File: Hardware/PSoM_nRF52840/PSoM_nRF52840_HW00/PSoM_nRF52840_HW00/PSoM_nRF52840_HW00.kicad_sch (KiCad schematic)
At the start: 0 parts

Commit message: started nrf52 schematic
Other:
- sheet 400_ESP32 renamed 400_nRF52840
- title: PSoM - ESP S3 -> PSoM - nRF52840

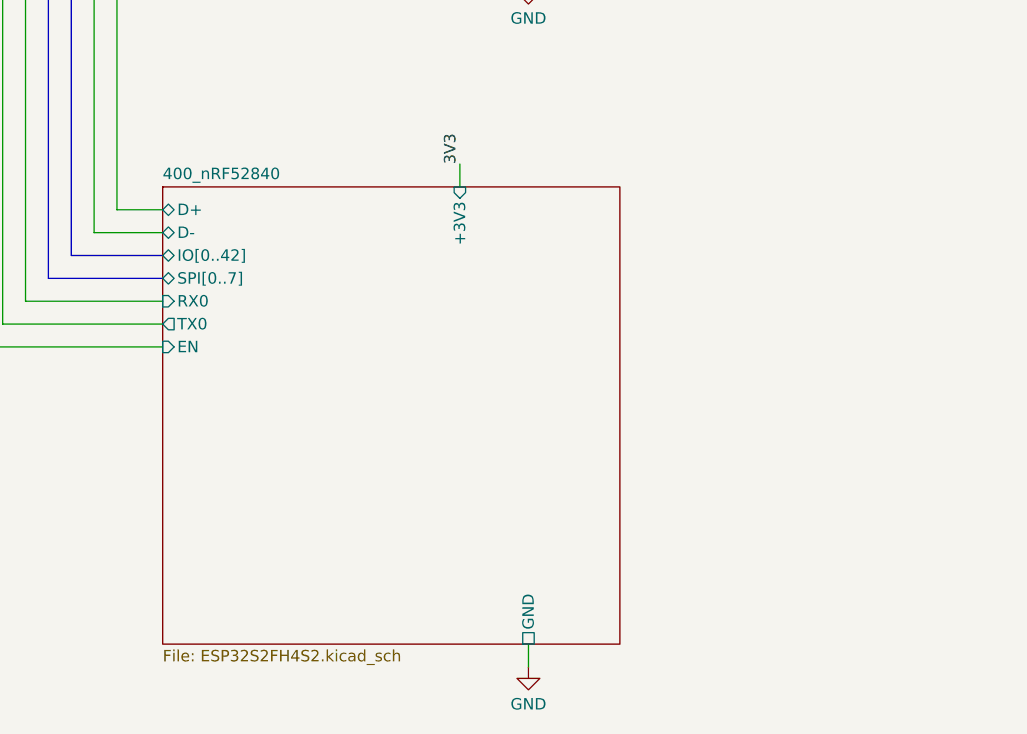
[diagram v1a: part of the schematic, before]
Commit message: nrf schematic ongoing
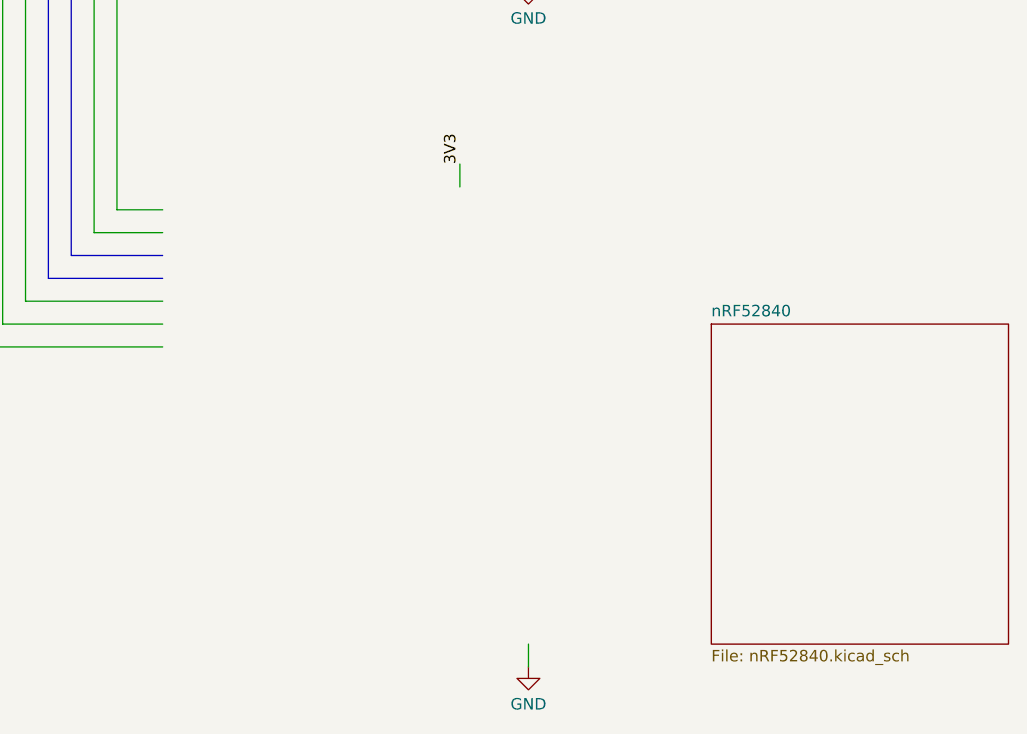
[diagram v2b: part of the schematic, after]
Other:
- removed sheet 400_nRF52840
- added sheet nRF52840 (nRF52840.kicad_sch)
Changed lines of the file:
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@@
 	)
 	(sheet
-		(at 127 101.6)
-		(size 50.8 50.8)
+		(at 187.96 116.84)
+		(size 33.02 35.56)
 		(fields_autoplaced yes)
 		(stroke
@@
 			(color 0 0 0 0.0000)
 		)
-		(property "Sheetname" "400_nRF52840"
-			(at 127 100.8884 0)
+		(property "Sheetname" "nRF52840"
+			(at 187.96 116.1284 0)
 			(effects
 				(font
@@
 			)
 		)
-		(property "Sheetfile" "ESP32S2FH4S2.kicad_sch"
-			(at 127 152.9846 0)
+		(property "Sheetfile" "nRF52840.kicad_sch"
+			(at 187.96 152.9846 0)
 			(effects
 				(font
@@
 			)
 		)
-		(pin "D-" bidirectional
-			(at 127 106.68 180)
-			(effects
-				(font
-					(size 1.27 1.27)
-				)
-				(justify left)
-			)
-		)
-		(pin "+3V3" input
-			(at 160.02 101.6 90)
-			(effects
-				(font
-					(size 1.27 1.27)
-				)
-				(justify right)
-			)
-		)
-		(pin "D+" bidirectional
-			(at 127 104.14 180)
-			(effects
-				(font
-					(size 1.27 1.27)
-				)
-				(justify left)
-			)
-		)
-		(pin "GND" passive
-			(at 167.64 152.4 270)
-			(effects
-				(font
-					(size 1.27 1.27)
-				)
-				(justify left)
-			)
-		)
-		(pin "IO[0..42]" bidirectional
-			(at 127 109.22 180)
-			(effects
-				(font
-					(size 1.27 1.27)
-				)
-				(justify left)
-			)
-		)
-		(pin "RX0" input
-			(at 127 114.3 180)
-			(effects
-				(font
-					(size 1.27 1.27)
-				)
-				(justify left)
-			)
-		)
-		(pin "TX0" output
-			(at 127 116.84 180)
-			(effects
-				(font
-					(size 1.27 1.27)
-				)
-				(justify left)
-			)
-		)
-		(pin "SPI[0..7]" bidirectional
-			(at 127 111.76 180)
-			(effects
-				(font
-					(size 1.27 1.27)
-				)
-				(justify left)
-			)
-		)
-		(pin "EN" input
-			(at 127 119.38 180)
-			(effects
-				(font
-					(size 1.27 1.27)
-				)
-				(justify left)
-			)
-		)

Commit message: working on schematic
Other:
- removed sheet 300_Power
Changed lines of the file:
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@@
 	)
 	(sheet
-		(at 187.96 116.84)
+		(at 142.24 104.14)
 		(size 33.02 35.56)
 		(fields_autoplaced yes)
@@
 		)
 		(property "Sheetname" "nRF52840"
-			(at 187.96 116.1284 0)
+			(at 142.24 103.4284 0)
 			(effects
 				(font
@@
 		)
 		(property "Sheetfile" "nRF52840.kicad_sch"
-			(at 187.96 152.9846 0)
+			(at 142.24 140.2846 0)
 			(effects
 				(font
@@
 				)
 			)
-		)
-	)
-	(sheet
-		(at 50.8 101.6)
-		(size 50.8 50.8)
-		(fields_autoplaced yes)
-		(stroke
-			(width 0.1524)
-			(type solid)
-		)
-		(fill
-			(color 0 0 0 0.0000)
-		)
-		(property "Sheetname" "300_Power"
-			(at 50.8 100.8884 0)
-			(effects
-				(font
-					(size 1.27 1.27)
-				)
-				(justify left bottom)
-			)
-		)
-		(property "Sheetfile" "Power.kicad_sch"
-			(at 50.8 152.9846 0)
-			(effects
-				(font
-					(size 1.27 1.27)
-				)
-				(justify left top)
-			)
-		)
-		(pin "+3V3" output
-			(at 88.9 101.6 90)
-			(effects
-				(font
-					(size 1.27 1.27)
-				)
-				(justify right)
-			)
-		)
-		(pin "VSYS" input
-			(at 91.44 101.6 90)
-			(effects
-				(font
-					(size 1.27 1.27)
-				)
-				(justify right)
-			)
-		)
-		(pin "GND" passive
-			(at 88.9 152.4 270)
-			(effects
-				(font
-					(size 1.27 1.27)
-				)
-				(justify left)
-			)
-		)
-		(instances
-			(project "PSoM_nRF52840_HW00"
-				(path "/14b8af2e-80ef-48c8-890f-5f81b4faa854"
-					(page "4")
-				)
-			)
